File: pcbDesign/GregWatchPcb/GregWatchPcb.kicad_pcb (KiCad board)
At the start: 2 copper layers, 35 parts, among them J1 AVR-ISP-6, SW1 SW_Push, SW2 SW_Push, SW3 SW_Push, SW4 SW_Push, U1 Nokia_5110_LCD, U2 ATmega328P-AU, U3 74HC14, Y1 16M

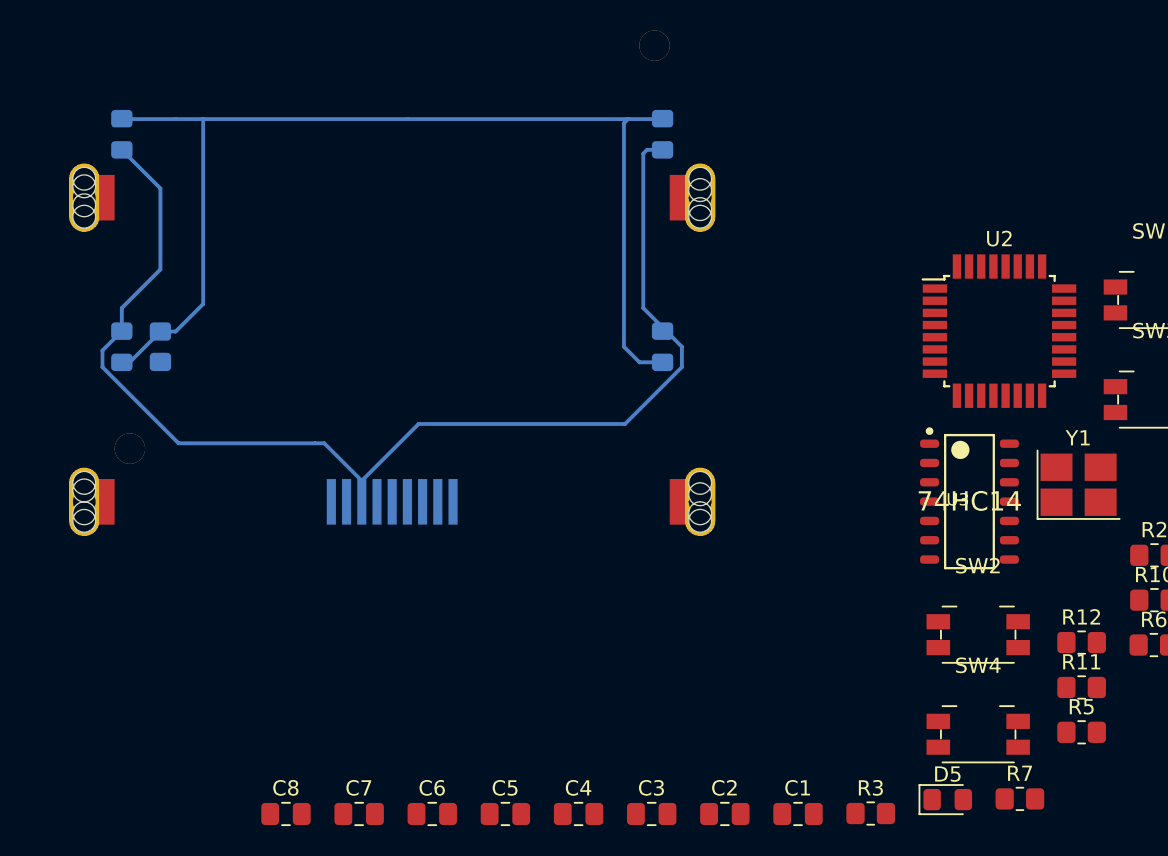
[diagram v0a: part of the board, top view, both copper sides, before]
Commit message: Move LEDs and flip capacitor and resistor to make sure things fit under the clip on screen
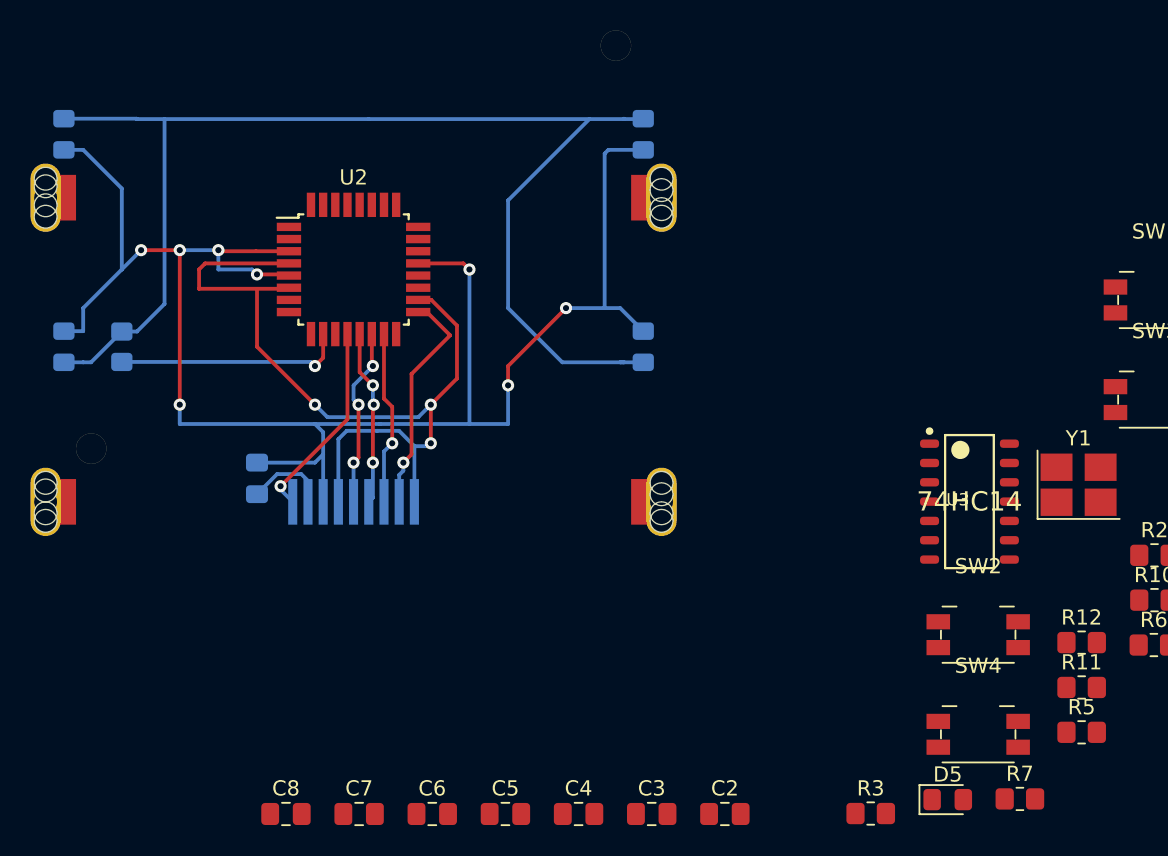
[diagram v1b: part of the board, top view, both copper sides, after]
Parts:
- C1: moved to B.Cu
- moved U2 42.7 mm to (135.9, 72.4)
- moved C1 41.9 mm to (129.5, 86.1), turned to 270 degrees
- moved D1 3.81 mm to (116.8, 77.5)
- moved D2 3.81 mm to (116.8, 63.5)
- moved U1 2.54 mm to (135.9, 90.2)
- moved R1 2.54 mm to (120.7, 77.5)
- moved D3 1.27 mm to (154.9, 63.5)
- moved D4 1.27 mm to (154.9, 77.5)
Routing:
- net +5V: track 0.00 -> 57.1 mm, vias 0 -> 3
- net GND: track 79.2 -> 118.5 mm, vias 0 -> 8
- net Net-(R1-Pad1): track 0.00 -> 15.1 mm, vias 0 -> 1
- net Net-(J1-Pad3): track 0.00 -> 15.1 mm, vias 0 -> 1
- net Net-(U1-Pad1): track 0.00 -> 13.2 mm, vias 0 -> 1
- net Net-(U1-Pad5): track 0.00 -> 11.9 mm, vias 0 -> 3
- net Net-(U1-Pad6): track 0.00 -> 11.5 mm, vias 0 -> 3
- net Net-(J1-Pad4): track 0.00 -> 11.5 mm, vias 0 -> 1
- net Net-(D1-Pad2): track 72.8 -> 83.8 mm
- net Net-(C1-Pad2): track 0.00 -> 5.46 mm

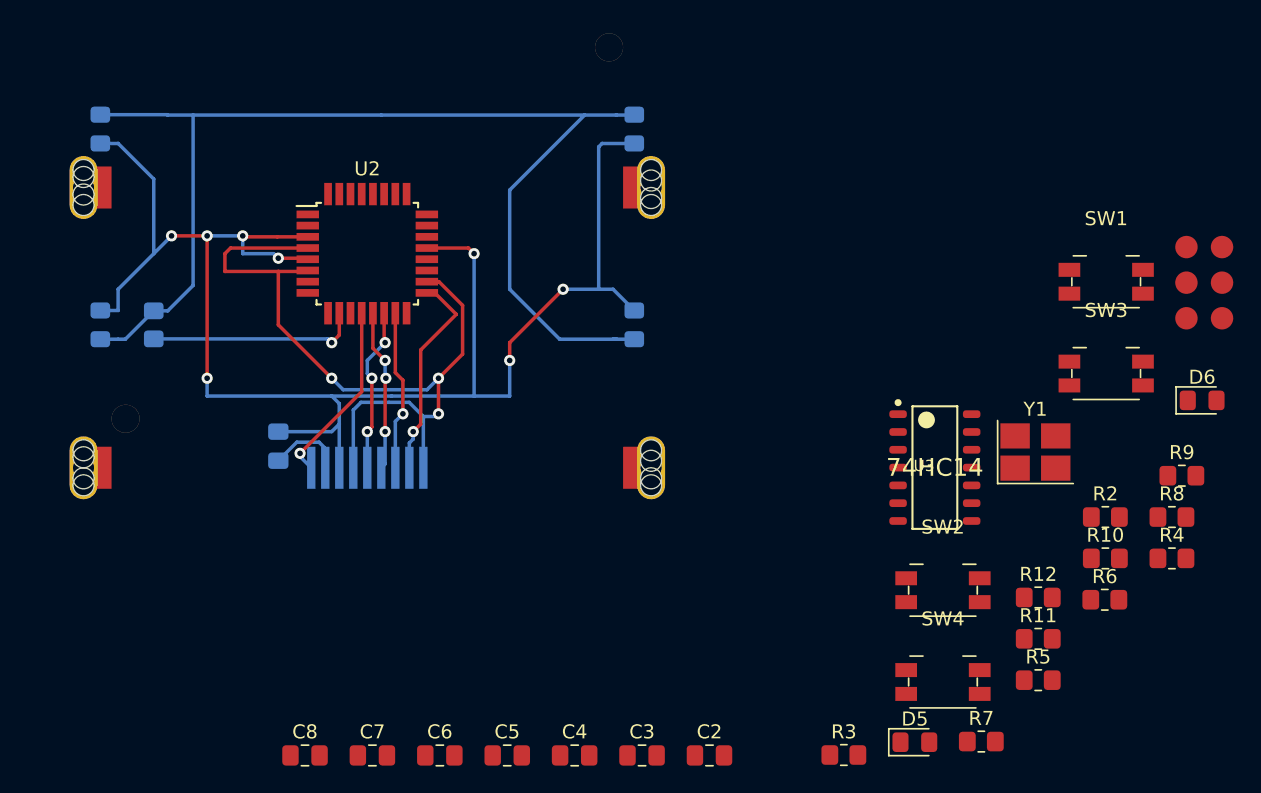
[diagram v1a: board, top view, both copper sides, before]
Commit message: Moved switched and ISP pad in place. Only partial connections so far.
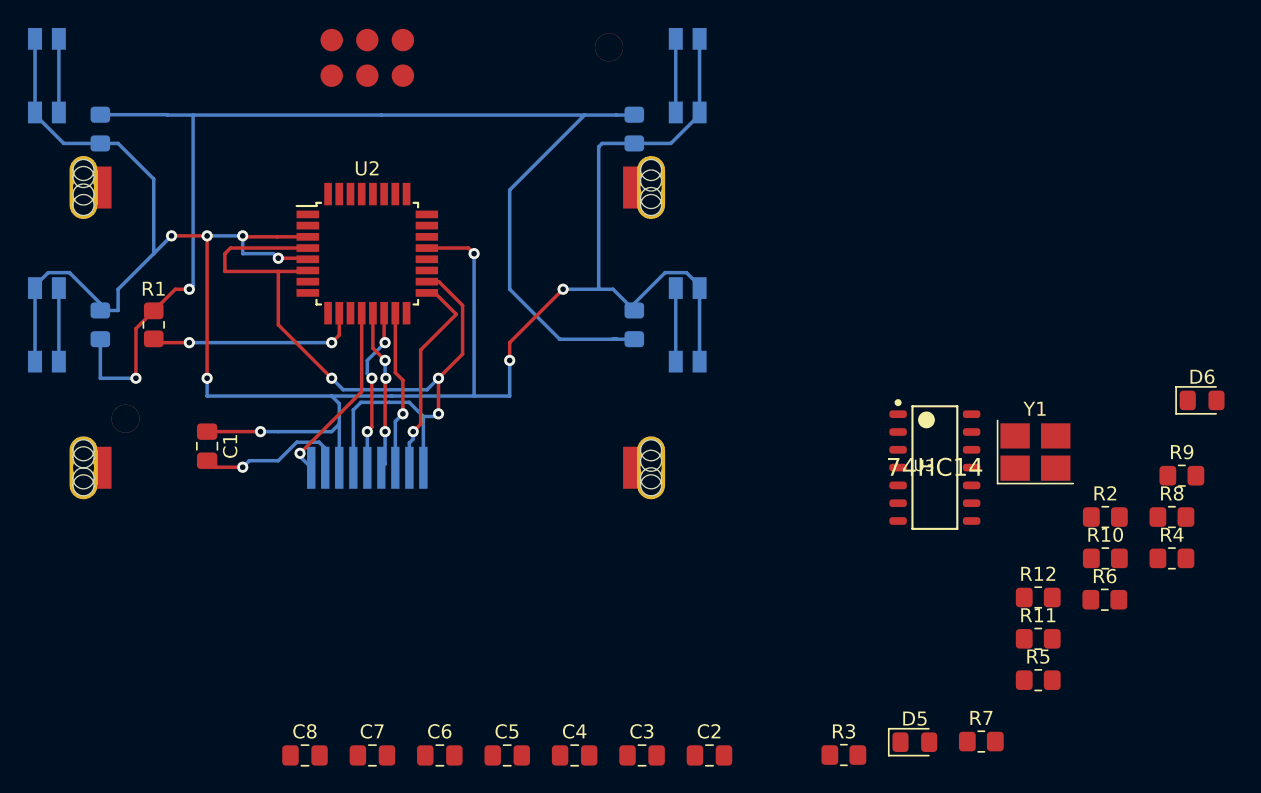
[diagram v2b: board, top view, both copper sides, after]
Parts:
- C1, R1: moved to F.Cu
- SW1, SW2, SW3, SW4: moved to B.Cu
- moved SW3 75.7 mm to (113.0, 77.5), turned to 270 degrees
- moved SW2 73.7 mm to (113.0, 59.7), turned to 270 degrees
- moved J1 57.8 mm to (138.4, 57.1), turned to 270 degrees
- moved SW1 33.3 mm to (158.8, 59.7), turned to 90 degrees
- moved SW4 31.3 mm to (158.8, 77.5), turned to 90 degrees
- moved C1 5.08 mm to (124.5, 86.1)
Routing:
- net GND: track 118.5 -> 169.2 mm, vias 8 -> 9
- net Net-(D1-Pad2): track 83.8 -> 89.8 mm, vias 0 -> 2
- net Net-(C1-Pad2): track 5.46 -> 10.9 mm, vias 0 -> 1
- net Net-(R6-Pad1): track 0.00 -> 5.25 mm
- net Net-(R5-Pad1): track 0.00 -> 5.25 mm
- net Net-(R11-Pad2): track 0.00 -> 5.25 mm
- net Net-(R10-Pad2): track 0.00 -> 5.25 mm
- net Net-(R1-Pad1): vias 1 -> 2

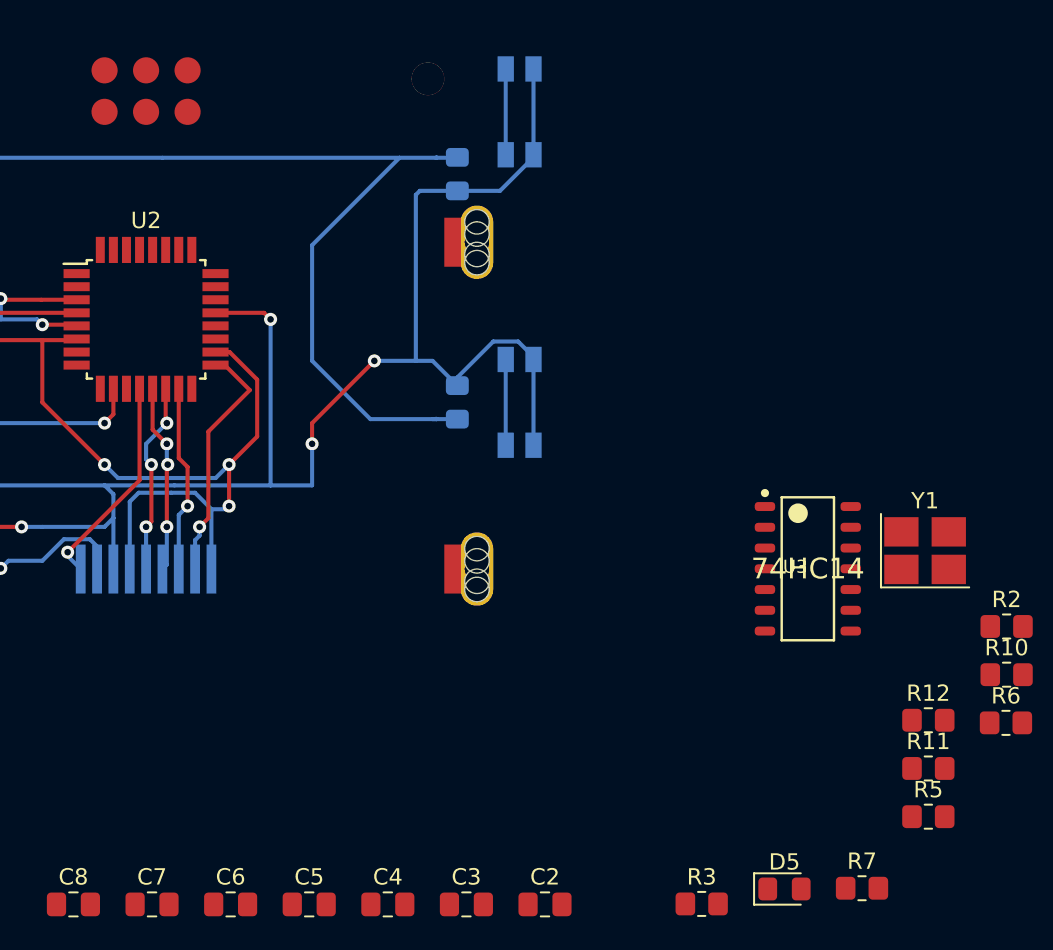
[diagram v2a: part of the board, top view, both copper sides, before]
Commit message: First button connected
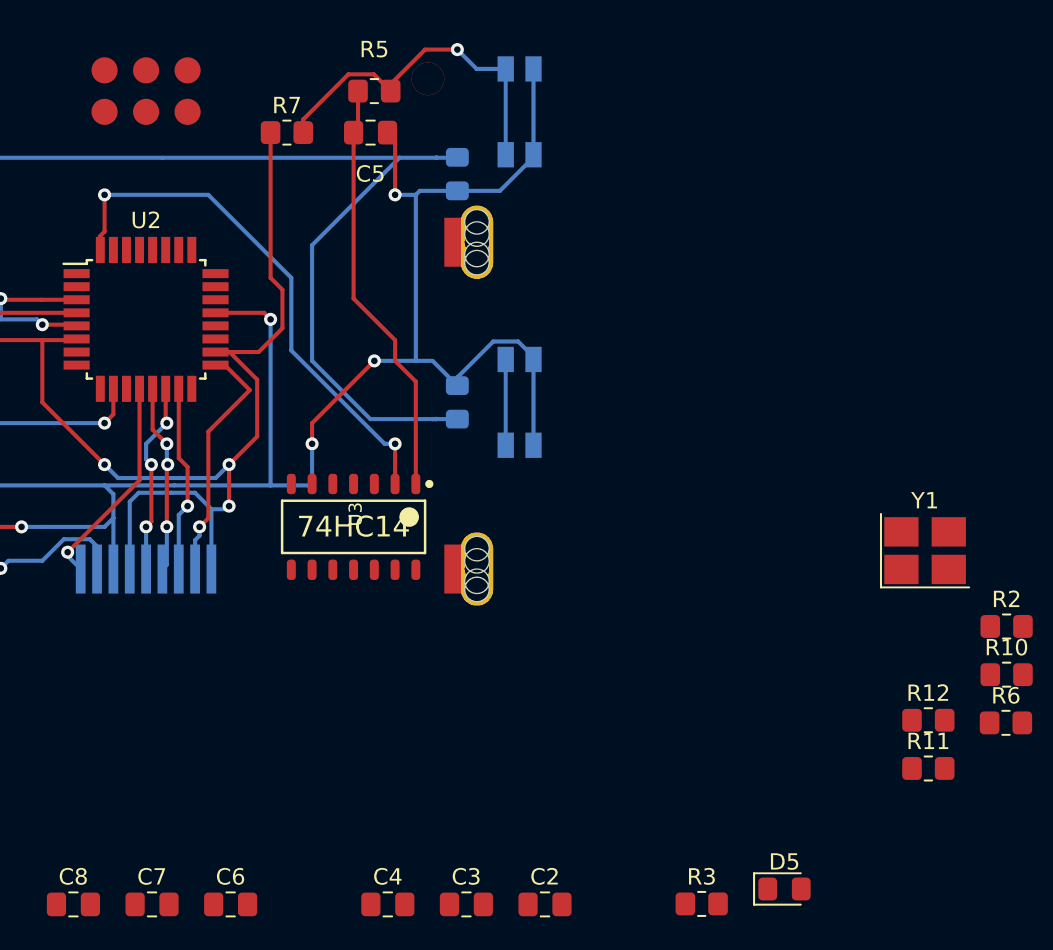
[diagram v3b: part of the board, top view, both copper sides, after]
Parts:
- moved R7 58.1 mm to (144.5, 61.0)
- moved R5 55.9 mm to (149.9, 58.4), turned to 180 degrees
- moved C5 47.4 mm to (149.6, 61.0)
- moved U3 27.9 mm to (148.6, 85.1), turned to 270 degrees
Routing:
- net Net-(U2-Pad32): track 0.00 -> 32.6 mm, vias 0 -> 2
- net Net-(C5-Pad1): track 0.00 -> 25.7 mm
- net Net-(R5-Pad1): track 5.25 -> 21.8 mm, vias 0 -> 1
- net +5V: track 57.1 -> 73.2 mm
- net GND: track 169.2 -> 174.5 mm, vias 9 -> 10

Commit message: Top two buttons connected
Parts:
- moved R6 78.3 mm to (120.4, 58.4)
- moved R8 75.2 mm to (124.5, 61.0), turned to 180 degrees
- moved C6 51.6 mm to (120.4, 61.0), turned to 180 degrees
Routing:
- net Net-(C6-Pad1): track 0.00 -> 56.3 mm, vias 0 -> 4
- net Net-(U2-Pad1): track 0.00 -> 48.2 mm, vias 0 -> 2
- net +5V: track 73.2 -> 92.3 mm
- net Net-(R6-Pad1): track 5.25 -> 18.5 mm, vias 0 -> 1
- net GND: track 174.5 -> 181.1 mm, vias 10 -> 11

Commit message: Connected the ICSP programmer pad
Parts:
- moved Y1 58.7 mm to (125.6, 77.3), turned to 270 degrees
- moved R1 1.27 mm to (119.4, 77.5)
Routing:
- net Net-(J1-Pad4): track 11.5 -> 106.8 mm
- net Net-(J1-Pad1): track 0.00 -> 86.1 mm, vias 0 -> 4
- net Net-(J1-Pad3): track 15.1 -> 94.9 mm
- net GND: track 181.1 -> 210.5 mm, vias 11 -> 14
- net +5V: track 92.3 -> 119.8 mm
- net Net-(C3-Pad2): track 0.00 -> 10.1 mm
- net Net-(C2-Pad2): track 0.00 -> 6.53 mm
- net Net-(R1-Pad1): track 15.1 -> 16.4 mm

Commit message: Connected the third button
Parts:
- moved R9 81.1 mm to (113.0, 83.8), turned to 270 degrees
- moved R10 67.5 mm to (121.9, 83.5), turned to 270 degrees
- moved C7 26.7 mm to (114.5, 92.7)
- moved R12 23.6 mm to (172.4, 76.2)
- moved R11 21.0 mm to (174.0, 81.3)
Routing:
- net Net-(U2-Pad2): track 0.00 -> 102.1 mm, vias 0 -> 4
- net Net-(C7-Pad1): track 0.00 -> 53.8 mm, vias 0 -> 2
- net Net-(R10-Pad2): track 5.25 -> 22.0 mm, vias 0 -> 1
- net GND: track 210.5 -> 222.5 mm
- net +5V: track 119.8 -> 122.8 mm
- net Net-(J1-Pad1): track 86.1 -> 86.7 mm

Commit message: Place and routed the power and IC components
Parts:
- D1, D2, D3, D4, SW1, SW2, SW3, SW4: moved to F.Cu
- moved R9 115.3 mm to (223.5, 50.8), turned to 0 degrees
- moved R10 110.4 mm to (227.3, 50.8), turned to 0 degrees
- moved R8 95.8 mm to (219.7, 50.8), turned to 0 degrees
- moved R6 92.0 mm to (212.1, 50.8)
- moved D6 91.6 mm to (109.2, 52.1)
- moved SW2 82.8 mm to (175.3, 114.3), turned to 0 degrees
- moved D5 81.9 mm to (109.2, 58.4)
- moved SW3 81.2 mm to (185.4, 114.3), turned to 0 degrees
- moved R1 78.3 mm to (193.0, 50.8), turned to 0 degrees
- moved C5 75.6 mm to (106.7, 123.2)
- moved R7 72.1 mm to (215.9, 50.8)
- moved R12 67.5 mm to (234.9, 50.8)
- moved SW1 66.6 mm to (196.8, 114.3), turned to 0 degrees
- moved R3 65.1 mm to (200.7, 50.8)
- moved R11 64.8 mm to (231.1, 50.8)
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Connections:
- Y1 pad 1: Net-(C2-Pad2) -> Net-(C3-Pad2)
- Y1 pad 2: Net-(C3-Pad2) -> Net-(C2-Pad2)
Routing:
- net +5V: track 122.8 -> 223.7 mm
- net Net-(J1-Pad4): track 106.8 -> 17.2 mm, vias 1 -> 2
- net Net-(D1-Pad2): track 89.3 -> 0.00 mm, vias 2 -> 0
- net Net-(J1-Pad1): track 86.7 -> 6.13 mm, vias 4 -> 0
- net Net-(J1-Pad3): track 94.9 -> 25.5 mm
- net Net-(U2-Pad9): track 0.00 -> 62.9 mm, vias 0 -> 2
- net Net-(C6-Pad1): track 56.3 -> 0.00 mm, vias 4 -> 0
- net Net-(C7-Pad1): track 53.8 -> 0.00 mm, vias 2 -> 0
- net Net-(U2-Pad2): track 102.1 -> 66.3 mm, vias 4 -> 2
- net GND: track 222.5 -> 256.9 mm, vias 14 -> 5
- net Net-(U2-Pad32): track 32.6 -> 5.60 mm, vias 2 -> 0
- net Net-(C5-Pad1): track 25.7 -> 0.00 mm
- net Net-(U2-Pad1): track 48.2 -> 22.6 mm
- net Net-(R10-Pad2): track 22.0 -> 0.00 mm, vias 1 -> 0
- net Net-(R5-Pad1): track 21.8 -> 0.00 mm, vias 1 -> 0
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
